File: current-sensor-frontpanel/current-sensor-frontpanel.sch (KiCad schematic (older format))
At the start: 8 parts

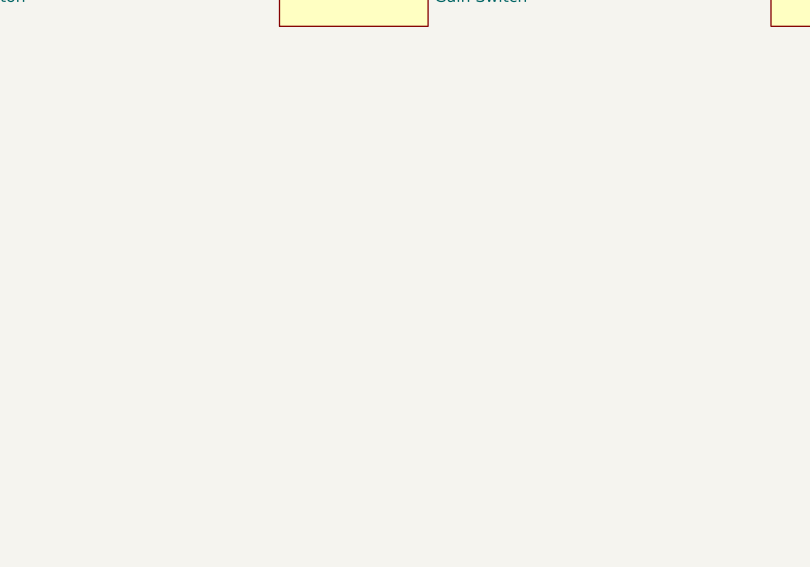
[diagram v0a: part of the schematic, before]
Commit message: complete front panel label
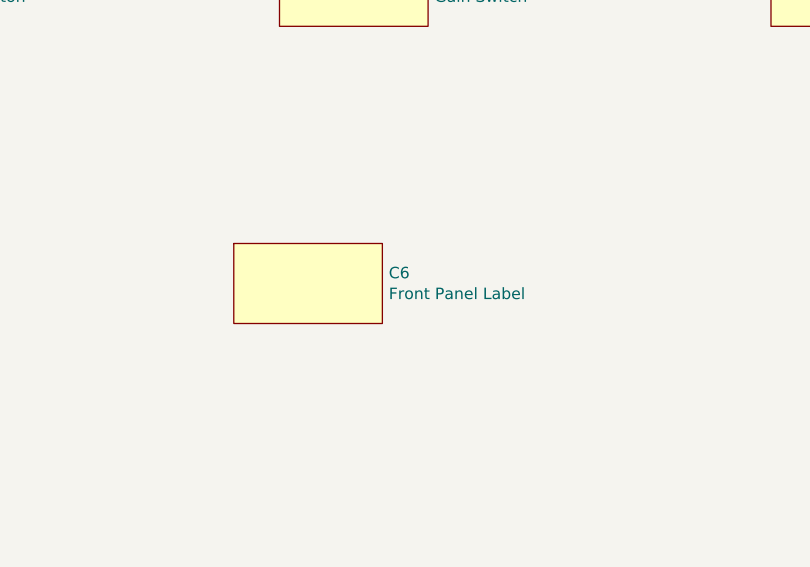
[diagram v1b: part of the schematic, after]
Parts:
- added C6: Front Panel Label, current-sensor:frontpanel, symbol Panel_Cutouts:Panel_Cutout
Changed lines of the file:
@@
+	1    0    0    -1
+$EndComp
+$Comp
+L Panel_Cutouts:Panel_Cutout C6
+U 1 1 5F936590
+P 3100 4350
+F 0 "C6" H 3778 4171 50  0000 L CNN
+F 1 "Front Panel Label" H 3778 4080 50  0000 L CNN
+F 2 "current-sensor:frontpanel" H 3100 4350 50  0001 C CNN
+F 3 "" H 3100 4350 50  0001 C CNN
+	1    3100 4350
 	1    0    0    -1
 $EndComp
